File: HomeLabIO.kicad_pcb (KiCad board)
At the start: 4 copper layers, 230 x 42 mm, 81 parts, among them J1 104031-0811, J2 HDMI_A, J3 Bus_M.2_Socket_M, J5 61900419521, J6 USB_C_Receptacle_USB2.0_16P, M2 CM4-GPIO, U1 MagJack-A70-112-331N126, U11 EMC2301, U13 TPD4EUSB30, U2 TPD4EUSB30, U3 TPD4EUSB30, U4 RT9742GGJ5, U5 74LVC1G07SE-7, U6 CP2102N-A02-GQFN24R, U7 AG5405, U8 AP3441SHE-7B

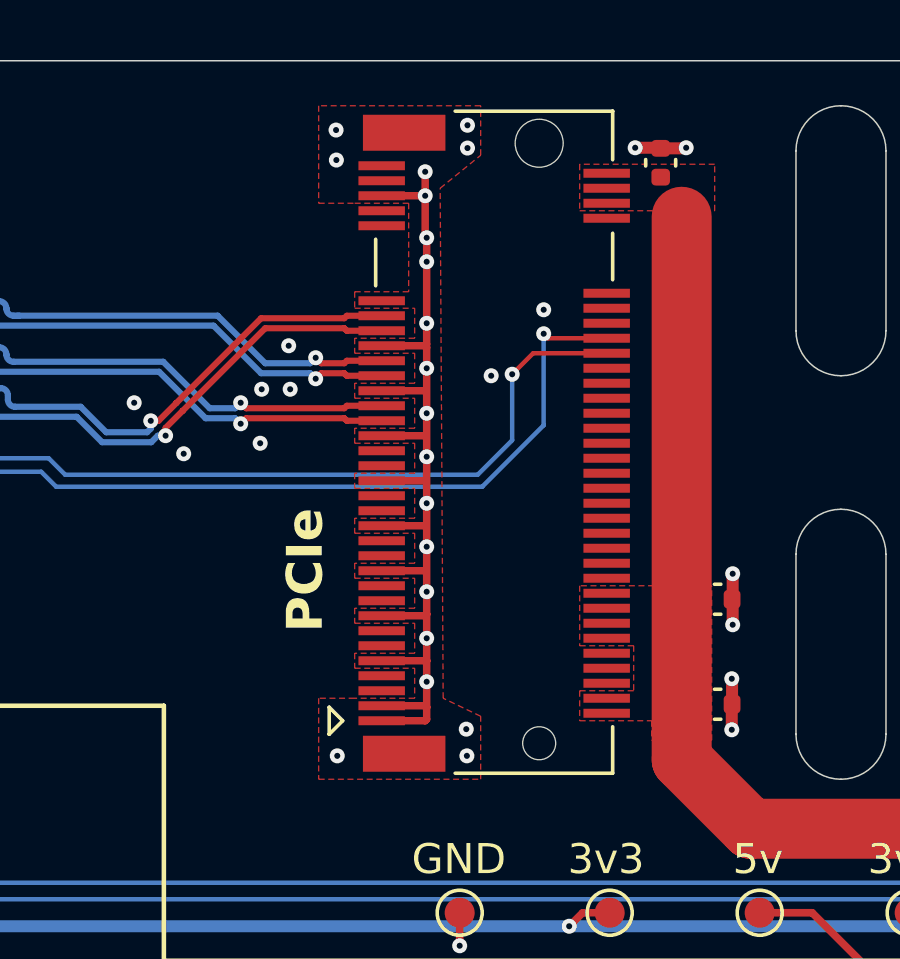
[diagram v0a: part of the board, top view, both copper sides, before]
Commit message: feat: NMVe led
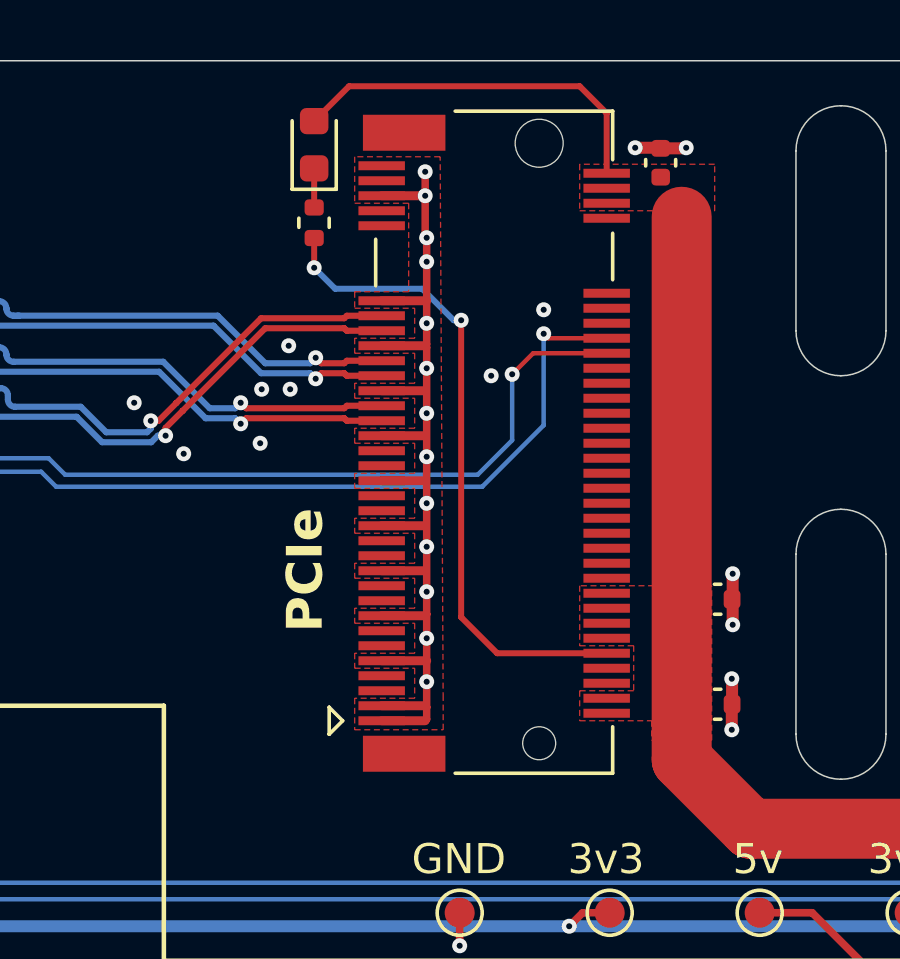
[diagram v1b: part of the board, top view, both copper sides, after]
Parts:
- added D7: LED, LED_SMD:LED_0603_1608Metric, F.Cu at (161.8, 67.4)
- added R6: 1k, Resistor_SMD:R_0402_1005Metric, F.Cu at (161.8, 70.0)
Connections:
- J3 pad 10: unconnected-(J3-DAS/~{DSS}/~{LED1}-Pad10) -> Net-(J3-DAS/~{DSS}/~{LED1})
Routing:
- net Net-(J3-DAS/~{DSS}/~{LED1}): track 0.00 -> 21.9 mm, vias 0 -> 2
- net +3.3V_PCIe: track 61.5 -> 74.1 mm
- net GND: track 131.0 -> 132.5 mm, vias 147 -> 140
- net Net-(D7-K): track 0.00 -> 1.30 mm

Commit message: chore: bump version to v0.2 (#13)
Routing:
- net +3.3V_PCIe: track 74.1 -> 81.3 mm
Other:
- board text added: "v0.2"
- board text removed: "v0.1"

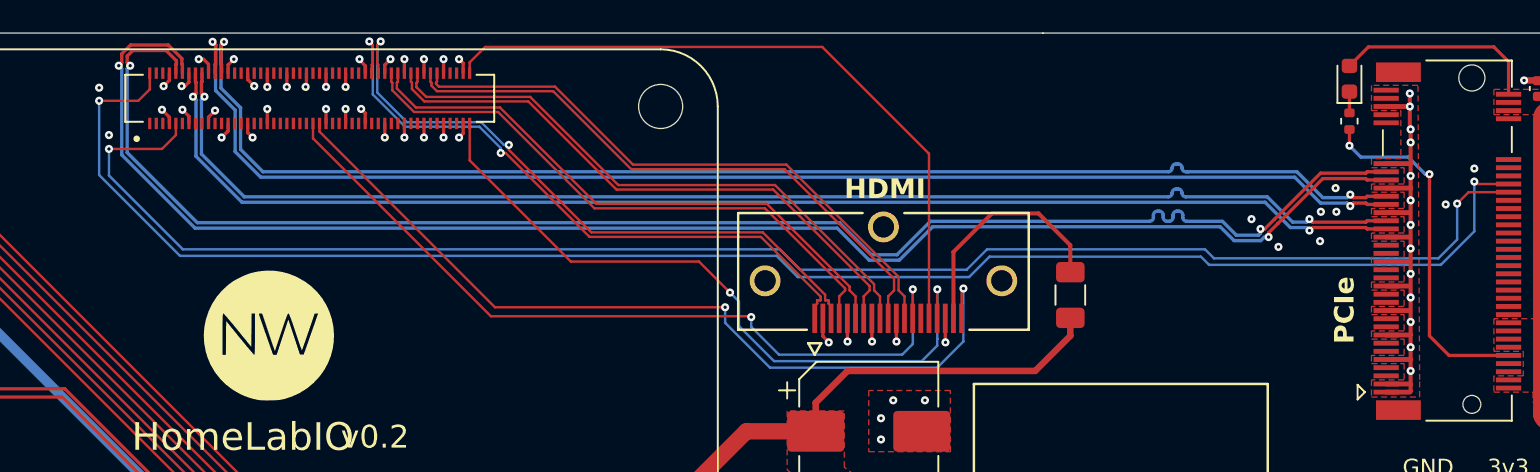
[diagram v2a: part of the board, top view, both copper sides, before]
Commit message: feat: move HDMI up
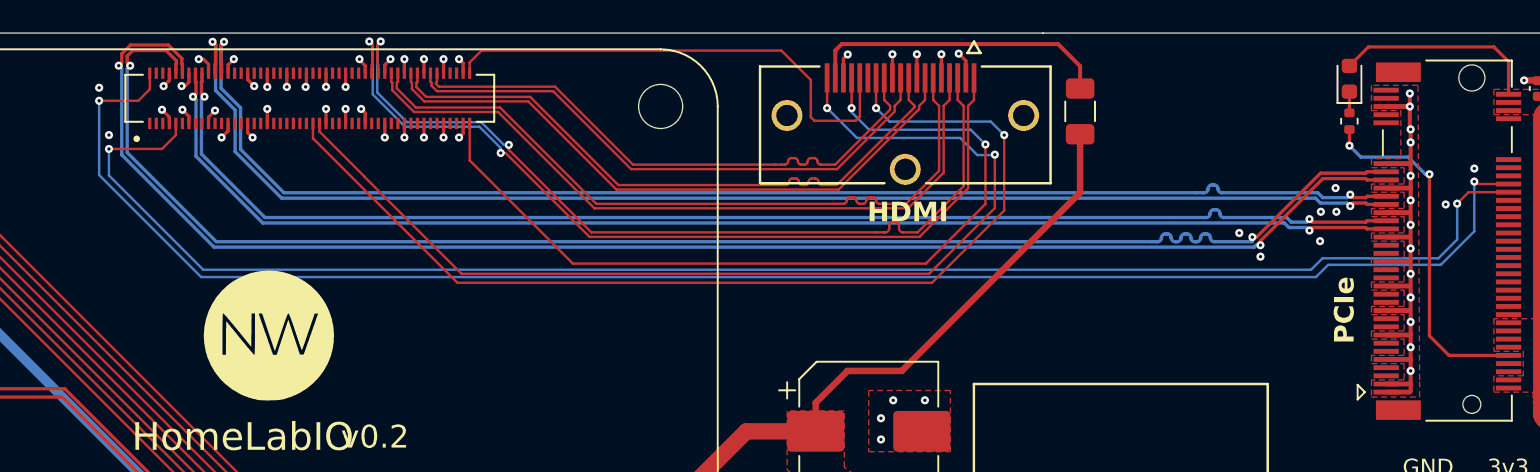
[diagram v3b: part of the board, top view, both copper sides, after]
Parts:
- moved F1 11.3 mm to (145.2, 69.4)
- moved J2 9.08 mm to (134.5, 70.2), turned to 0 degrees
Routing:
- net /CM4_HighSpeed/HDMI.CEC: track 48.9 -> 63.8 mm
- net /CM4_HighSpeed/HDMI.D2_P: track 39.7 -> 53.8 mm
- net /CM4_HighSpeed/HDMI.D2_N: track 39.7 -> 53.8 mm
- net /CM4_HighSpeed/HDMI.SCL: track 42.0 -> 30.5 mm
- net /CM4_HighSpeed/HDMI.HPD: track 52.3 -> 63.8 mm
- net /CM4_HighSpeed/HDMI.SDA: track 42.5 -> 52.8 mm
- net /CM4_HighSpeed/HDMI.D1_P: track 35.8 -> 44.7 mm
- net /CM4_HighSpeed/HDMI.D1_N: track 35.8 -> 44.6 mm
- net +5V: track 176.0 -> 182.7 mm
- net Net-(J2-+5V): track 14.7 -> 18.8 mm
- net /CM4_HighSpeed/HDMI.D0_P: track 36.2 -> 38.7 mm
- net /CM4_HighSpeed/HDMI.D0_N: track 36.2 -> 38.7 mm
- net /CM4_HighSpeed/HDMI.CLK_N: track 36.6 -> 34.9 mm
- net /CM4_HighSpeed/HDMI.CLK_P: track 36.6 -> 35.0 mm
- net /CM4_HighSpeed/PCIe.CLK_P: track 94.5 -> 93.1 mm
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
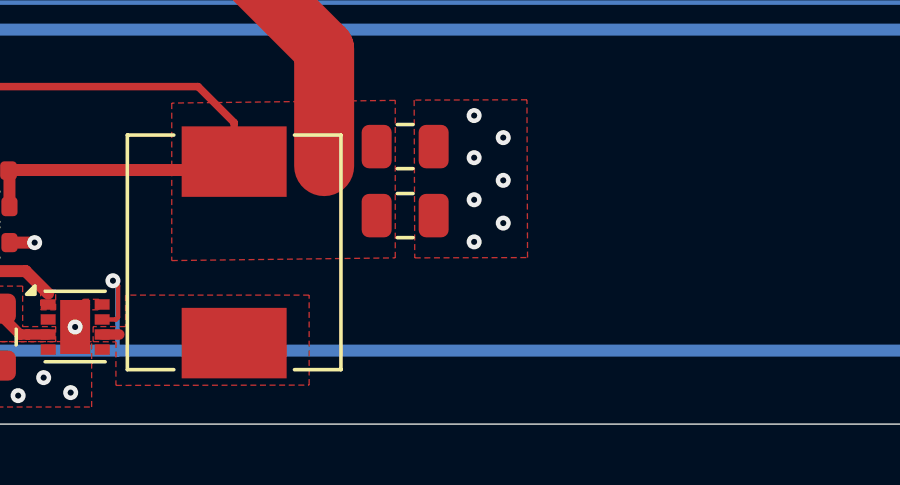
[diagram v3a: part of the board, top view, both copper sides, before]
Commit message: feat: PCIe power LED (#15)
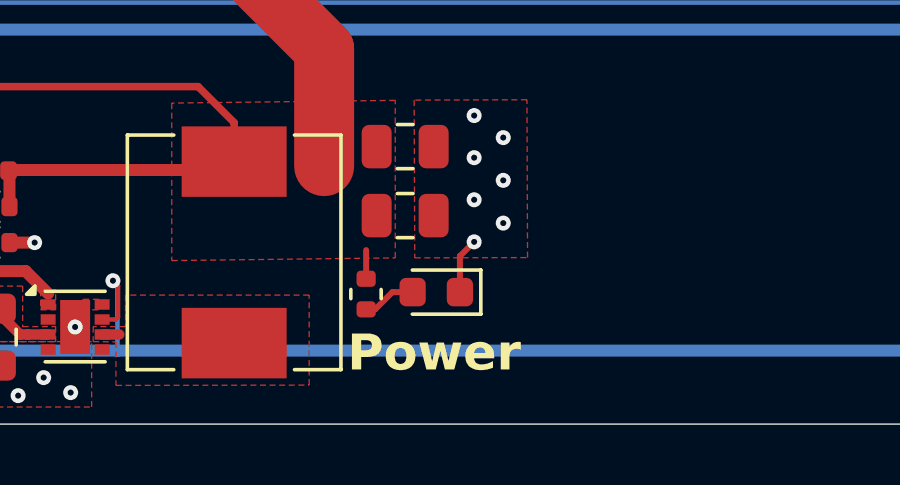
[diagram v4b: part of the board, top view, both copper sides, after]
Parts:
- added D8: LED, LED_SMD:LED_0603_1608Metric, F.Cu at (199.3, 102.2)
- added R7: 1k, Resistor_SMD:R_0402_1005Metric, F.Cu at (196.9, 102.3)
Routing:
- net GND: track 132.7 -> 134.6 mm
- net Net-(D8-A): track 0.00 -> 1.79 mm
- net +3.3V_PCIe: track 81.3 -> 82.3 mm
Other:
- board text added: "Power"

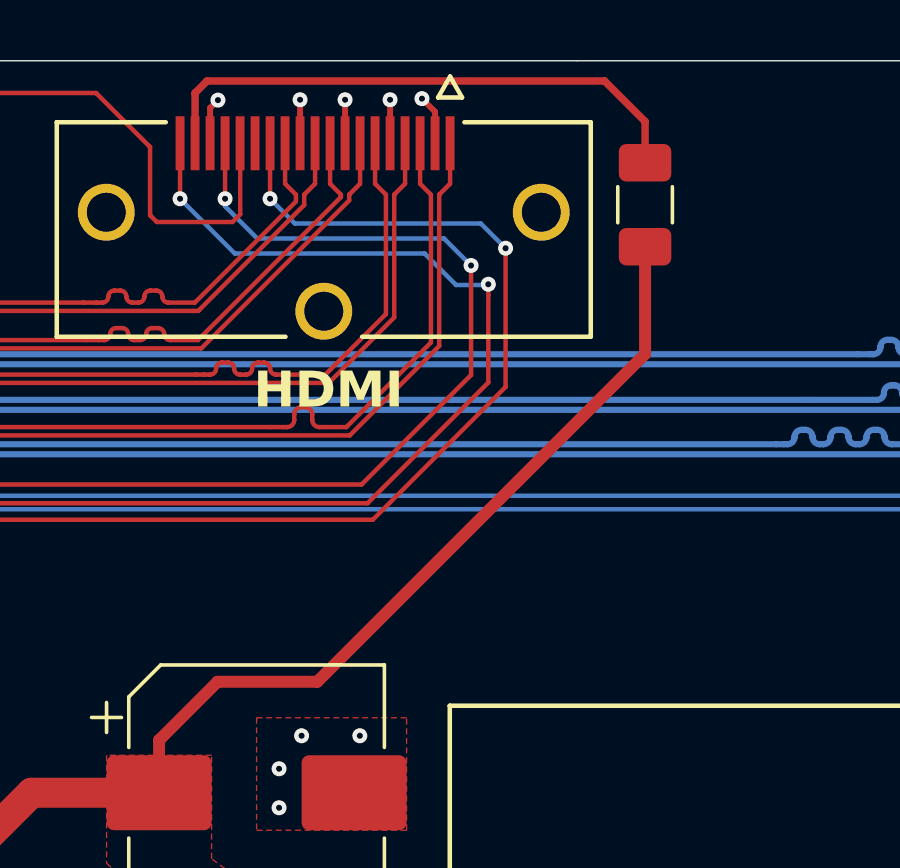
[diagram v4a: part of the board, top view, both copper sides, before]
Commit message: fix: DFM issues (#16)
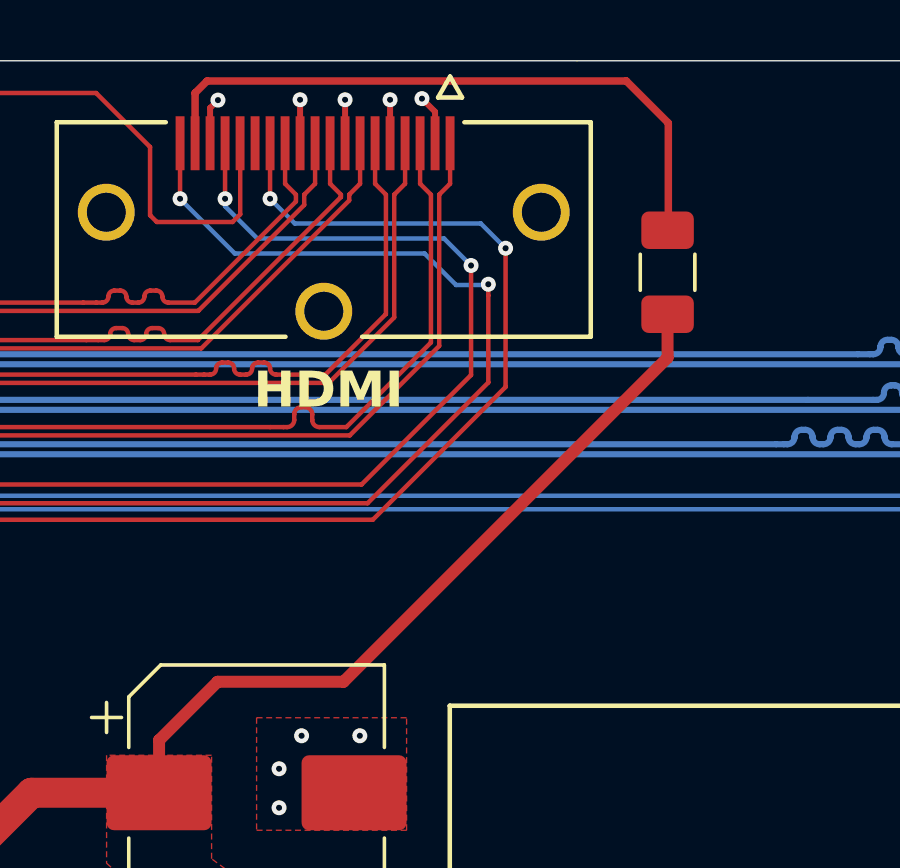
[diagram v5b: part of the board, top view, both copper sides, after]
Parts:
- moved F1 2.37 mm to (146.0, 71.7)
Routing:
- net Net-(J2-+5V): track 18.8 -> 21.8 mm
- net +5V: track 182.7 -> 181.3 mm
